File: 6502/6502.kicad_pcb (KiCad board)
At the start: 2 copper layers, 188.3 x 192.4 mm, 56 parts, among them J1 Conn_01x08, J10 Conn_02x20_Odd_Even, J11 Mini-DIN-6, J12 Conn_02x20_Odd_Even, J13 Jack-DC, J14 Conn_01x02, J2 Conn_01x08, J3 Conn_01x03, J4 Conn_02x20_Odd_Even, J5 Conn_01x08, J6 Conn_01x05, J7 Conn_02x20_Odd_Even, J8 Conn_01x02, J9 Conn_01x02, Q1 FQP47P06, SW1 SW_Push, SW2 SW_Push, U1 74LS08, U10 LM7805_TO220, U2 74LS154, U3 28C256, U4 ATF22V10C, U5 65C02S, U6 AS6C4008-55PCN, U7 6522, U8 6522, U9 NHD-0420H1Z, X1 ACO-4MHz

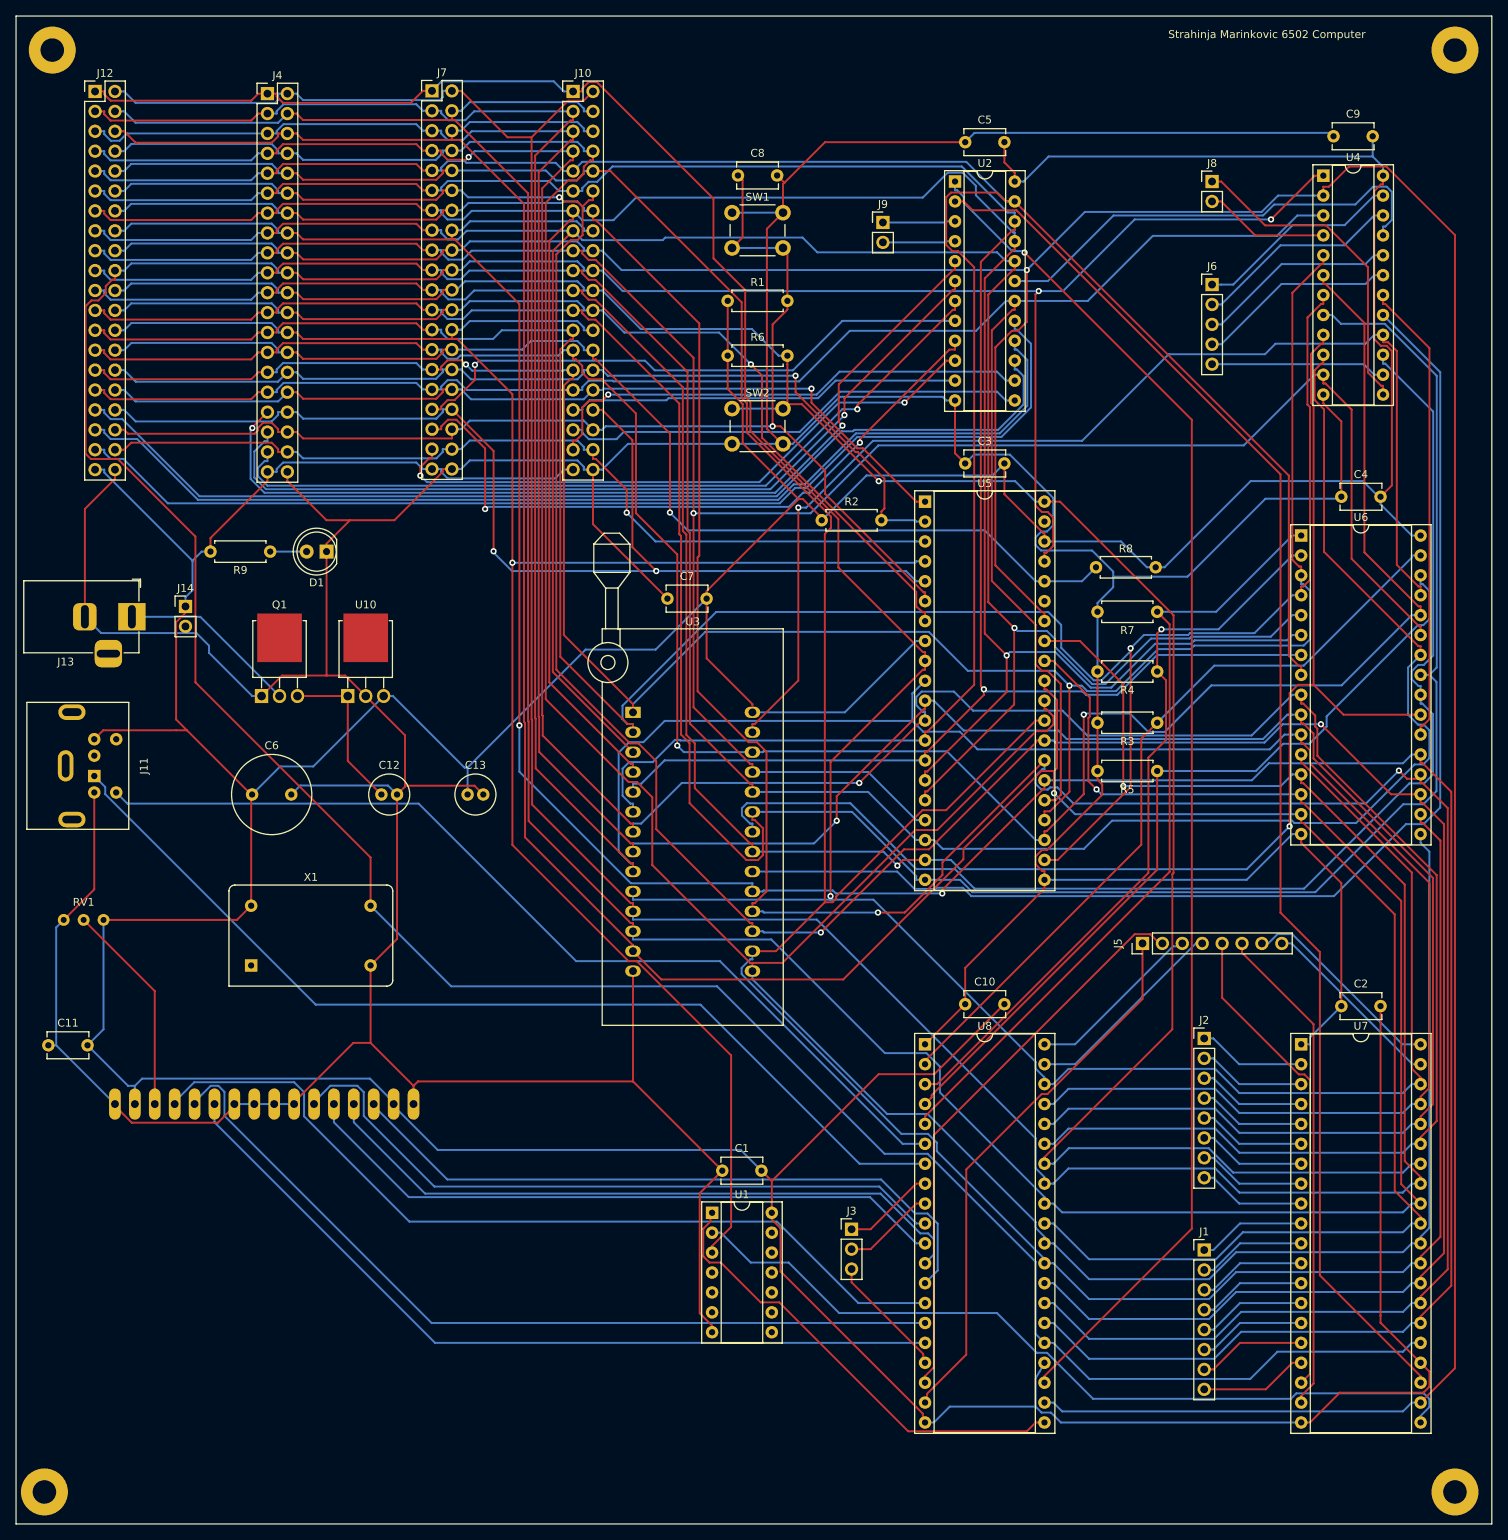
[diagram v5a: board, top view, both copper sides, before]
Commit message: fixed decoder circuit
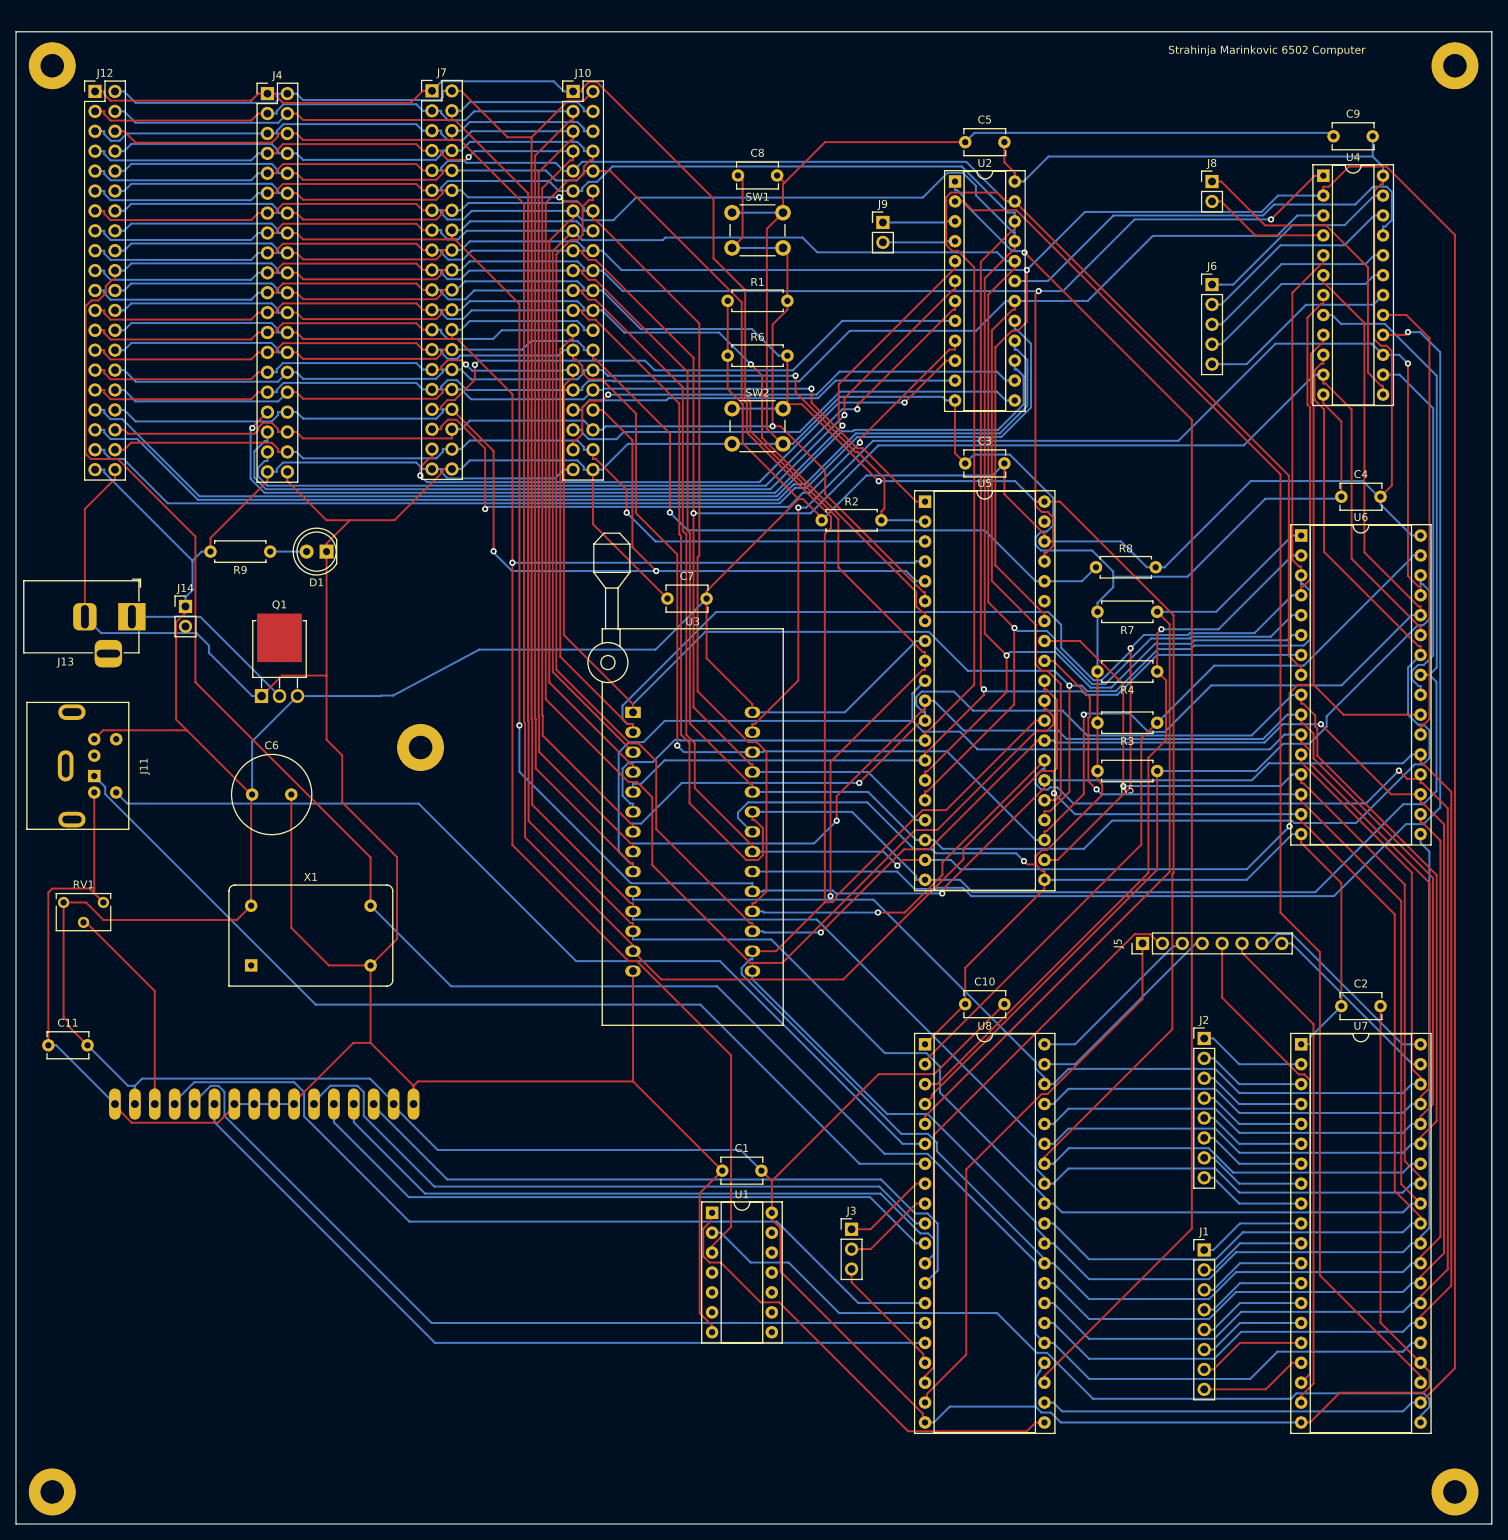
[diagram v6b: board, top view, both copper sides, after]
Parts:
- removed C12, C13: 1uF, Capacitor_THT:C_Radial_D5.0mm_H11.0mm_P2.00mm
- removed the REF** at (133.0, 75.0)
- removed the REF** at (132.0, 259.0)
- removed the REF** at (312.0, 75.0)
- removed U10: LM7805_TO220, Package_TO_SOT_THT:TO-251-3-1EP_Horizontal_TabDown
- added REF**: MountingHole_3mm_Pad, MountingHole:MountingHole_3mm_Pad, F.Cu at (312.0, 77.0)
- added REF**: MountingHole_3mm_Pad, MountingHole:MountingHole_3mm_Pad, F.Cu at (133.0, 77.0)
- added REF**: MountingHole_3mm_Pad, MountingHole:MountingHole_3mm_Pad, F.Cu at (133.0, 259.0)
- added REF**: MountingHole_3mm_Pad, MountingHole:MountingHole_3mm_Pad, F.Cu at (180.0, 164.0)
- RV1: footprint 6502Computer:10 kOhms 12 Watt Square Cermet Potentiometer -> Potentiometer_THT:Potentiometer_Bourns_3266W_Vertical
- moved RV1 3.37 mm to (139.5, 183.8)
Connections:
- Q1 pad 3: Net-(C12-Pad1) -> +5V
- U3 pad 22: OE -> GND
- U4 pad 14: decode4 -> OE
- U4 pad 15: OE -> WE
- U4 pad 16: WE -> ROM_CS
- U4 pad 17: ROM_CS -> RAM_CS
- U4 pad 18: RAM_CS -> decode4
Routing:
- net OE: track 162.1 -> 46.9 mm
- net GND: track 793.7 -> 846.9 mm, vias 0 -> 1
- net Net-(C12-Pad1): track 20.8 -> 0.00 mm
- net decode4: track 22.4 -> 25.5 mm
- net WE: track 150.8 -> 149.2 mm, vias 1 -> 2
- net RAM_CS: track 59.3 -> 58.4 mm
- net ROM_CS: track 159.8 -> 160.5 mm, vias 0 -> 1
- net +5V: track 843.7 -> 844.4 mm
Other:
- board size 188.3 x 192.4 mm -> 188.3 x 190.4 mm

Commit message: updated pcb
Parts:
- removed the J8 at (281.0, 91.8)
- removed the J9 at (239.0, 97.0)
- removed REF** (x5): MountingHole_3mm_Pad, MountingHole:MountingHole_3mm_Pad
- J6: value Conn_01x05 -> Conn_01x03; footprint Connector_PinHeader_2.54mm:PinHeader_1x05_P2.54mm_Vertical -> Connector_PinHeader_2.54mm:PinHeader_1x03_P2.54mm_Vertical
- moved C1 82.5 mm to (172.5, 149.5)
- moved U1 82.5 mm to (171.2, 154.9)
- moved J5 73.3 mm to (243.6, 256.5)
- moved J12 51.2 mm to (133.7, 194.5), turned to 90 degrees
- moved R9 39.5 mm to (161.0, 178.5)
- moved C9 31.7 mm to (265.0, 89.5)
- moved U4 31.7 mm to (263.7, 94.5)
- moved D1 31.0 mm to (158.5, 168.5)
- moved C4 29.0 mm to (269.5, 139.5)
- moved U6 29.0 mm to (264.4, 144.4)
- moved C2 28.0 mm to (269.5, 197.0)
- moved U7 28.0 mm to (264.4, 201.9)
- moved J1 27.5 mm to (252.5, 228.1)
- moved J2 27.5 mm to (252.5, 201.1)
- moved C6 22.5 mm to (152.0, 191.5)
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- renumbered J12 to J10, J13 to J11, J14 to J12, J10 to J8, J11 to J9
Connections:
- J10 pad 33: dev13 -> IO12
- J10 pad 35: dev14 -> IO13
- J10 pad 37: dev15 -> IO14
- J10 pad 38: PHI1O -> +5V
- J10 pad 39: +5V -> IO15
- J4 pad 33: dev4 -> IO0
- J4 pad 35: dev5 -> IO1
- J4 pad 37: dev6 -> IO2
- J4 pad 38: PHI1O -> +5V
- J4 pad 39: +5V -> IO3
- J7 pad 33: dev7 -> IO4
- J7 pad 35: dev8 -> IO5
- J7 pad 37: dev9 -> IO6
- J7 pad 38: PHI1O -> +5V
- J7 pad 39: +5V -> IO7
- J8 pad 33: dev10 -> IO8
- J8 pad 35: dev11 -> IO9
- J8 pad 37: dev12 -> IO10
- J8 pad 38: PHI1O -> +5V
- J8 pad 39: +5V -> IO11
- U2 pad 1: VIA1_CS -> IO0
- U2 pad 10: dev9 -> IO9
- U2 pad 11: dev10 -> IO10
- U2 pad 13: dev11 -> IO11
- U2 pad 14: dev12 -> IO12
- U2 pad 15: dev13 -> IO13
- U2 pad 16: dev14 -> IO14
- U2 pad 17: dev15 -> IO15
- U2 pad 2: VIA2_CS -> IO1
- U2 pad 3: dev2 -> IO2
- U2 pad 4: dev3 -> IO3
- U2 pad 5: dev4 -> IO4
- U2 pad 6: dev5 -> IO5
- U2 pad 7: dev6 -> IO6
- U2 pad 8: dev7 -> IO7
- U2 pad 9: dev8 -> IO8
- U4 pad 13: EXT_IN1 -> unconnected-(U4-Pad13)
- U4 pad 18: decode4 -> VIA1_CS
- U4 pad 19: decode3 -> VIA2_CS
- U4 pad 4: EXT_IN2 -> unconnected-(U4-Pad4)
- U5 pad 3: PHI1O -> unconnected-(U5-Pad3)
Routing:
- net GND: track 846.9 -> 682.8 mm
- net dev15: track 139.6 -> 0.00 mm
- net dev14: track 137.0 -> 0.00 mm
- net dev13: track 134.3 -> 0.00 mm
- net IO13: track 0.00 -> 125.8 mm
- net IO14: track 0.00 -> 118.1 mm
- net IO12: track 0.00 -> 117.2 mm, vias 0 -> 1
- net dev4: track 116.7 -> 0.00 mm, vias 2 -> 0
- net IO15: track 0.00 -> 115.4 mm
- net PHI1O: track 113.9 -> 0.00 mm, vias 1 -> 0
- net dev5: track 109.7 -> 0.00 mm, vias 1 -> 0
- net dev6: track 104.0 -> 0.00 mm, vias 1 -> 0
- net IO1: track 0.00 -> 101.1 mm, vias 0 -> 1
- net IO3: track 0.00 -> 100.4 mm
- net IO2: track 0.00 -> 100.0 mm, vias 0 -> 1
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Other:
- board size 188.3 x 190.4 mm -> 158.8 x 181.4 mm

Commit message: worked on pcb
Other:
- board size 158.8 x 181.4 mm -> 158.8 x 183.4 mm
